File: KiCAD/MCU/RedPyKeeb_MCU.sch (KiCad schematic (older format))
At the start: 22 parts, among them J0 Conn_01x04, J1 Conn_01x36, J2 Conn_01x04, U1 MCP23S17-E/SO, U2 MCP23S17-E/SO, U3 TXB0104D, U4 TXB0104D, U5 TXS0104ED, U6 SN74HC595DW, U7 TXS0104ED

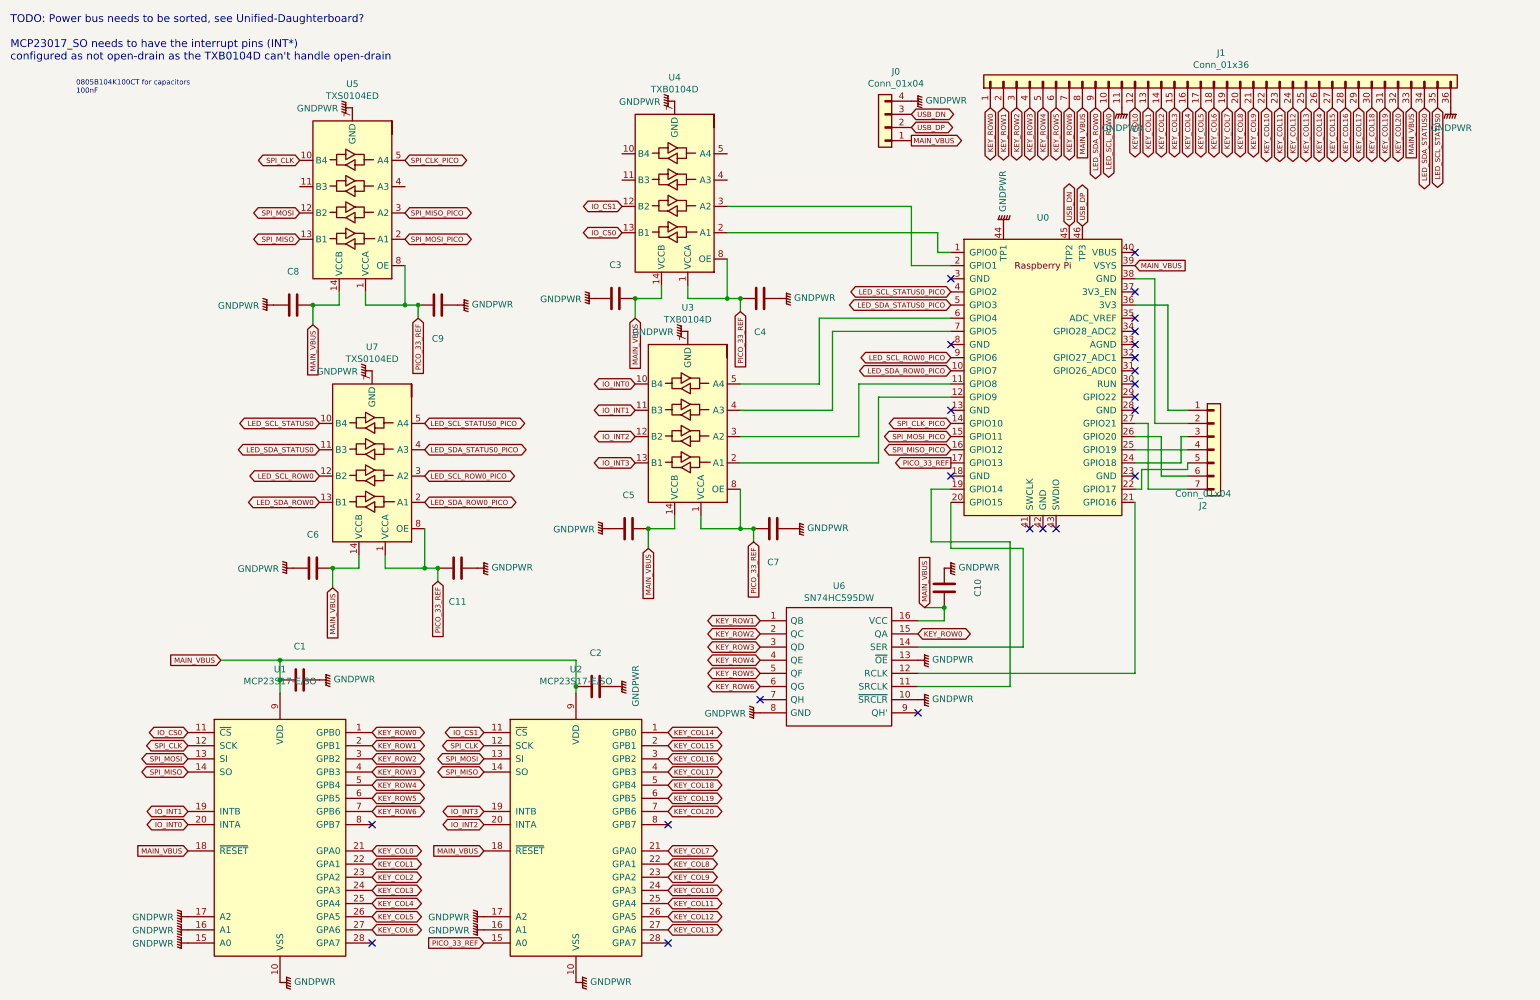
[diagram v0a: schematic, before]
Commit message: This is as-is before I test out a teensy MCU instead of the pico..
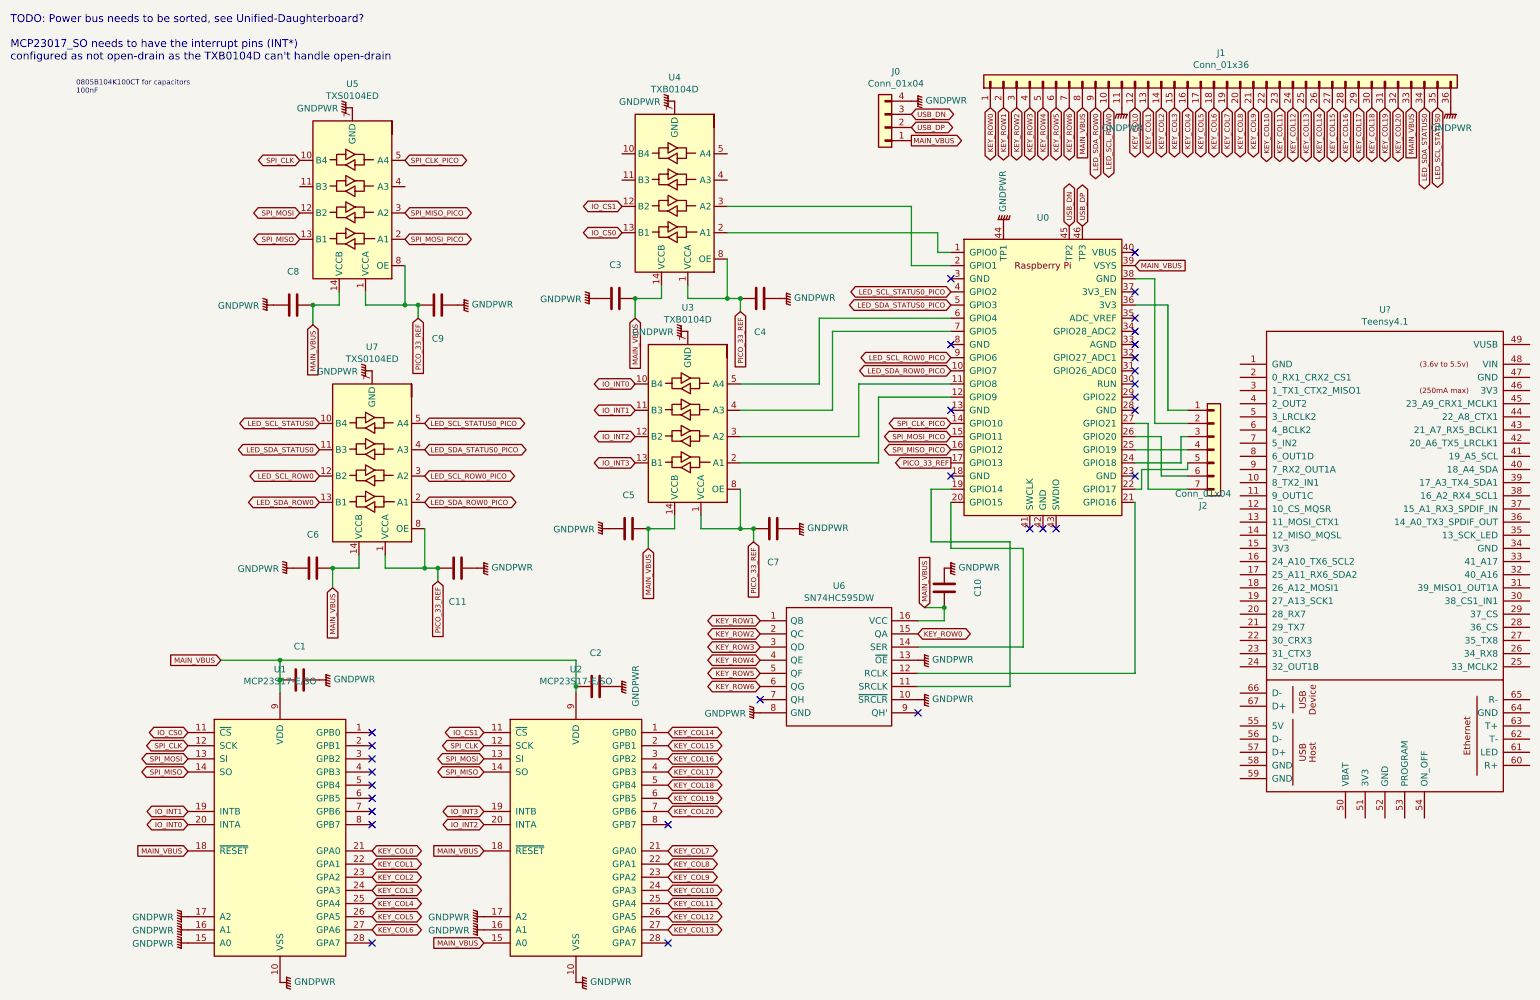
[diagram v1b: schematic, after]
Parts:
- added U?: Teensy4.1, teensy.pretty:Teensy41, symbol teensy:Teensy4.1
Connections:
- net KEY_ROW0: no longer U1.1 (GPB0)
- net KEY_ROW1: no longer U1.2 (GPB1)
- net KEY_ROW2: no longer U1.3 (GPB2)
- net KEY_ROW3: no longer U1.4 (GPB3)
- net KEY_ROW4: no longer U1.5 (GPB4)
- net KEY_ROW5: no longer U1.6 (GPB5)
- net KEY_ROW6: no longer U1.7 (GPB6)
- net MAIN_VBUS: now also U2.15 (A0)
- net PICO_33_REF: no longer U2.15 (A0)
- no-connect marks 24 -> 31
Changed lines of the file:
@@
 NoConn ~ 7250 2650
 NoConn ~ 8650 1950
-Text GLabel 2850 6100 2    39   BiDi ~ 0
-KEY_ROW5
-Text GLabel 2850 6000 2    39   BiDi ~ 0
-KEY_ROW4
-Text GLabel 2850 5900 2    39   BiDi ~ 0
-KEY_ROW3
-Text GLabel 2850 5800 2    39   BiDi ~ 0
-KEY_ROW2
-Text GLabel 2850 5700 2    39   BiDi ~ 0
-KEY_ROW1
-Text GLabel 2850 5600 2    39   BiDi ~ 0
-KEY_ROW0
 Text GLabel 5100 6700 2    39   BiDi ~ 0
 KEY_COL9
@@
 Text GLabel 2850 6500 2    39   BiDi ~ 0
 KEY_COL0
-Text GLabel 2850 6200 2    39   BiDi ~ 0
-KEY_ROW6
 Text GLabel 5100 6900 2    39   BiDi ~ 0
 KEY_COL11
@@
 Text GLabel 5100 6200 2    39   BiDi ~ 0
 KEY_COL20
-Text GLabel 3700 7200 0    39   Input ~ 0
-PICO_33_REF
 NoConn ~ 5100 7200
 NoConn ~ 5100 6300
@@
 Text GLabel 3250 3850 2    39   BiDi ~ 0
 LED_SDA_ROW0_PICO
+Text GLabel 3700 7200 0    39   Input ~ 0
+MAIN_VBUS
+NoConn ~ 2850 6200
+NoConn ~ 2850 6100
+NoConn ~ 2850 6000
+NoConn ~ 2850 5900
+NoConn ~ 2850 5800
+NoConn ~ 2850 5700
+NoConn ~ 2850 5600
+$Comp
+L teensy:Teensy4.1 U?
+U 1 1 609A8ABE
+P 10550 4950
+F 0 "U?" H 10550 7515 50  0000 C CNN
+F 1 "Teensy4.1" H 10550 7424 50  0000 C CNN
+F 2 "teensy.pretty:Teensy41" H 10150 5350 50  0001 C CNN
+F 3 "" H 10150 5350 50  0001 C CNN
+	1    10550 4950
+	1    0    0    -1
+$EndComp
 $EndSCHEMATC
